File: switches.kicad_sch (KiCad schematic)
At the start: 31 parts, among them J5 BM07B-SRSS-TB, SW1 B3FS-1052, SW2 291V1022F832AB, SW3 PEC164220F-S0024, SW4 MS-22C01-G010, U4 MCP23S17_ML

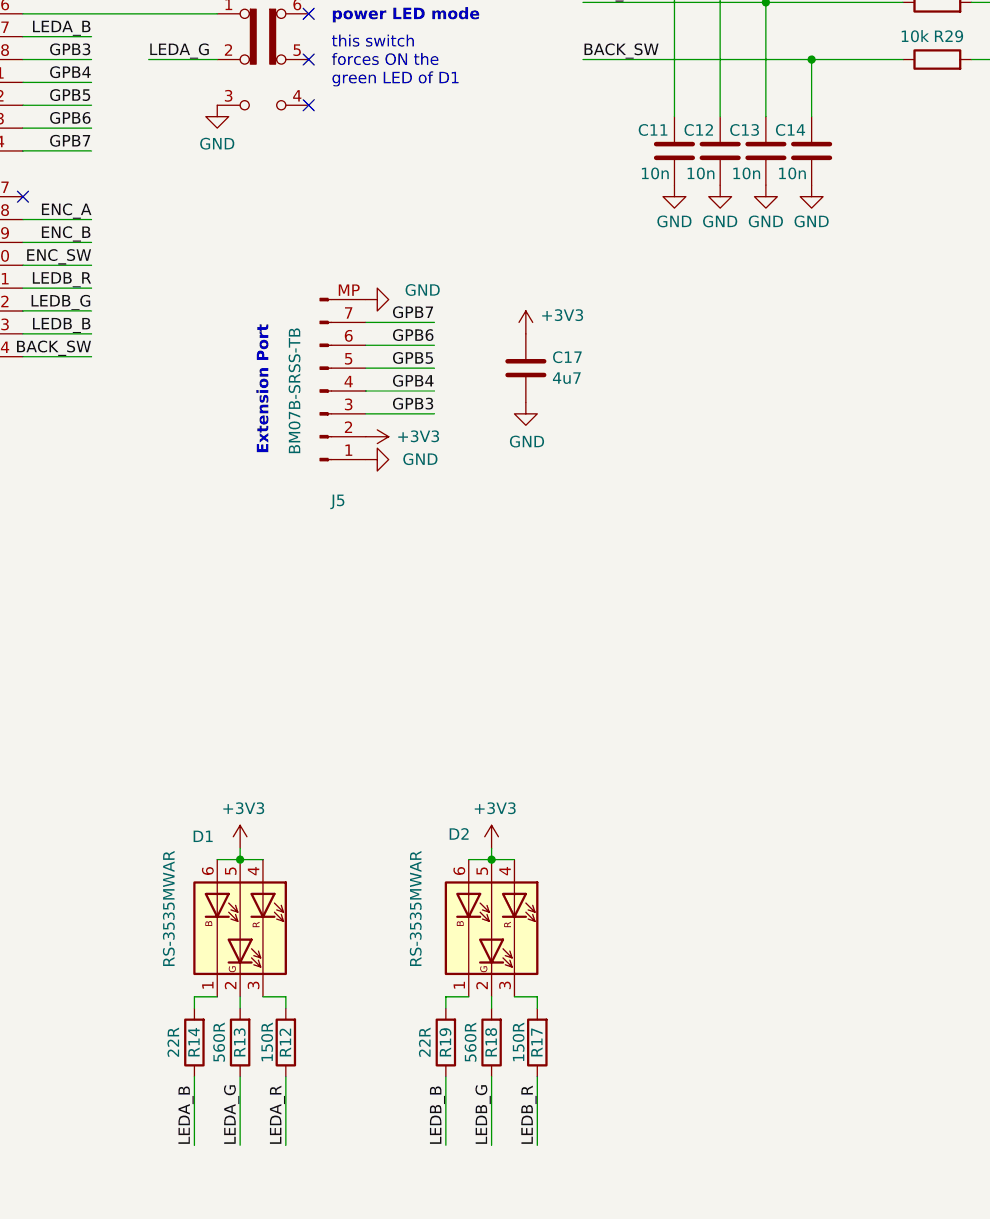
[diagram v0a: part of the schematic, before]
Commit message: rev1, port to kicad 10
  * revise LED resistor values. They were much to bright.
  * Change debouncing filter cap. from 10 nF to 100 nF
  * change to kicad 10
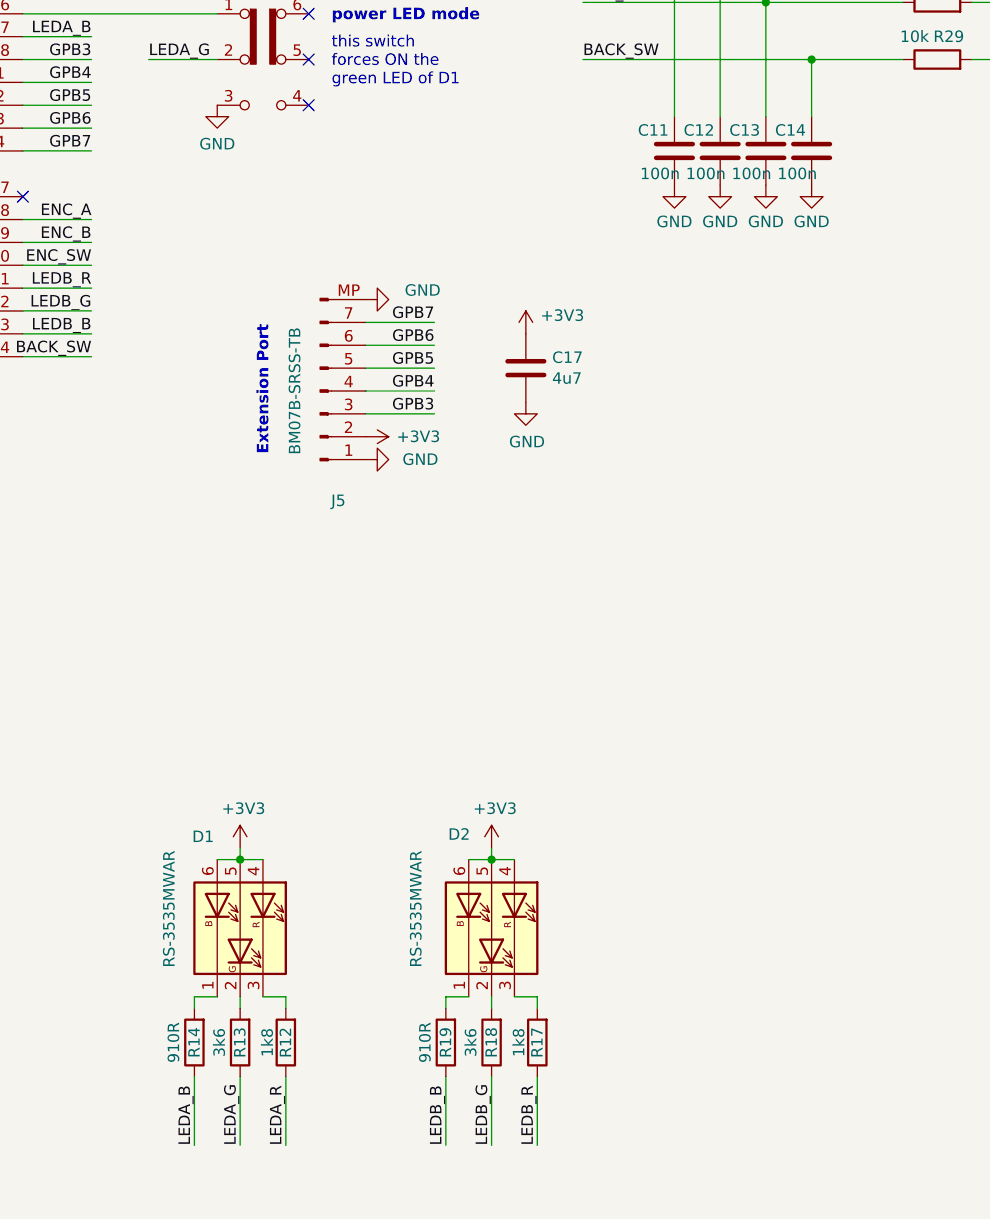
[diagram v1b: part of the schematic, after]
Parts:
- C11, C12, C13, C14: value 10n -> 100n
- R12, R17: value 150R -> 1k8
- R13, R18: value 560R -> 3k6
- R14, R19: value 22R -> 910R
